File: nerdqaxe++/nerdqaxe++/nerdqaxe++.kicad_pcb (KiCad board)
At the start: 6 copper layers, 89 x 165 mm, 244 parts, among them J1 XT30, J2 Conn_01x06, M1 Fan_4pin, M2 Fan_4pin, U10 CSD95472Q5MC, U19 BM1370_mode1, U20 BM1370_mode1, U25 BM1370_mode1, U26 BM1370_mode1, U3 TPS53647, U30 T-Display-S3, U32 EMC2302-1, U33 TXU0102-DCU, U35 TXU0304PW, U36 MCP1824T-1202E, U37 TMP1075, U38 TMP1075, U4 CSD95472Q5MC, U6 AP3211, U7 MCP1824T-0802E, U8 25MHz, U9 CSD95472Q5MC

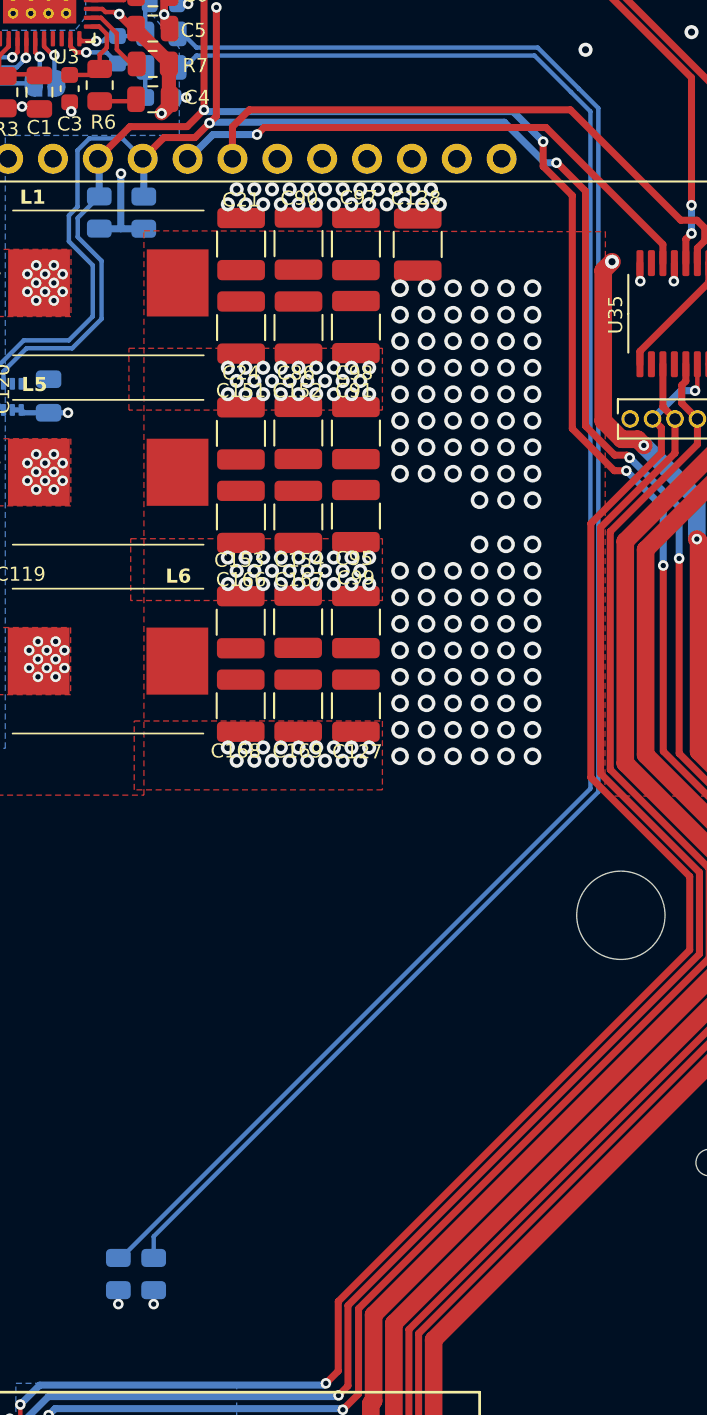
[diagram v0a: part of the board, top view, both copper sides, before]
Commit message: Nerdqaxe++ rev6.1.2PM
- Vsense resistors back to their original place
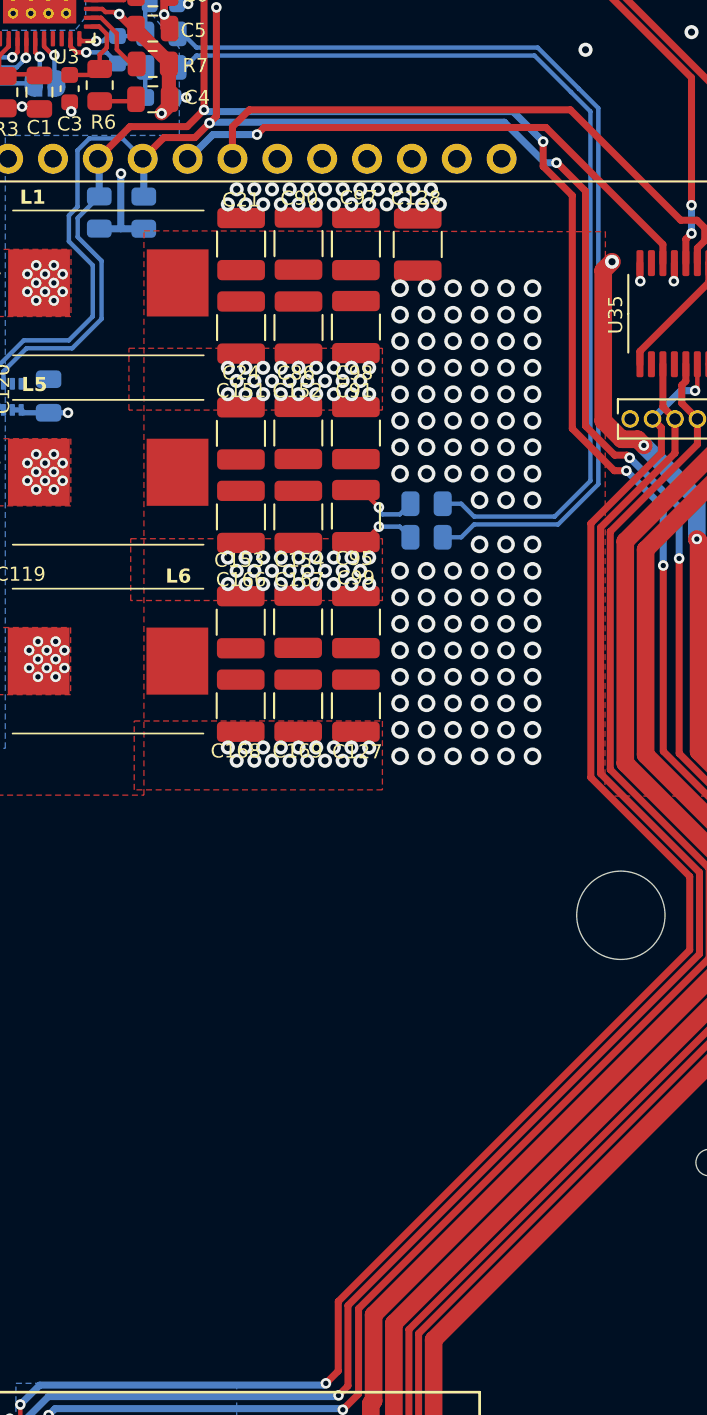
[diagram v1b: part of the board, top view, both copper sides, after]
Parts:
- moved R29 47.0 mm to (112.0, 67.7), turned to 180 degrees
- moved R30 44.5 mm to (112.0, 69.6), turned to 180 degrees
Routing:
- net /Power/VSENSE+: track 101.2 -> 55.4 mm
- net /Power/VSENSE-: track 101.3 -> 56.9 mm
- net GND: track 138.2 -> 141.9 mm
- net VDD: track 0.79 -> 4.02 mm
